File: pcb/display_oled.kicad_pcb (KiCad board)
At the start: 2 copper layers, 38.1 x 19.6 mm, 4 parts, among them J1 Molex-50511, Q1 AO3413, U1 SSD1306

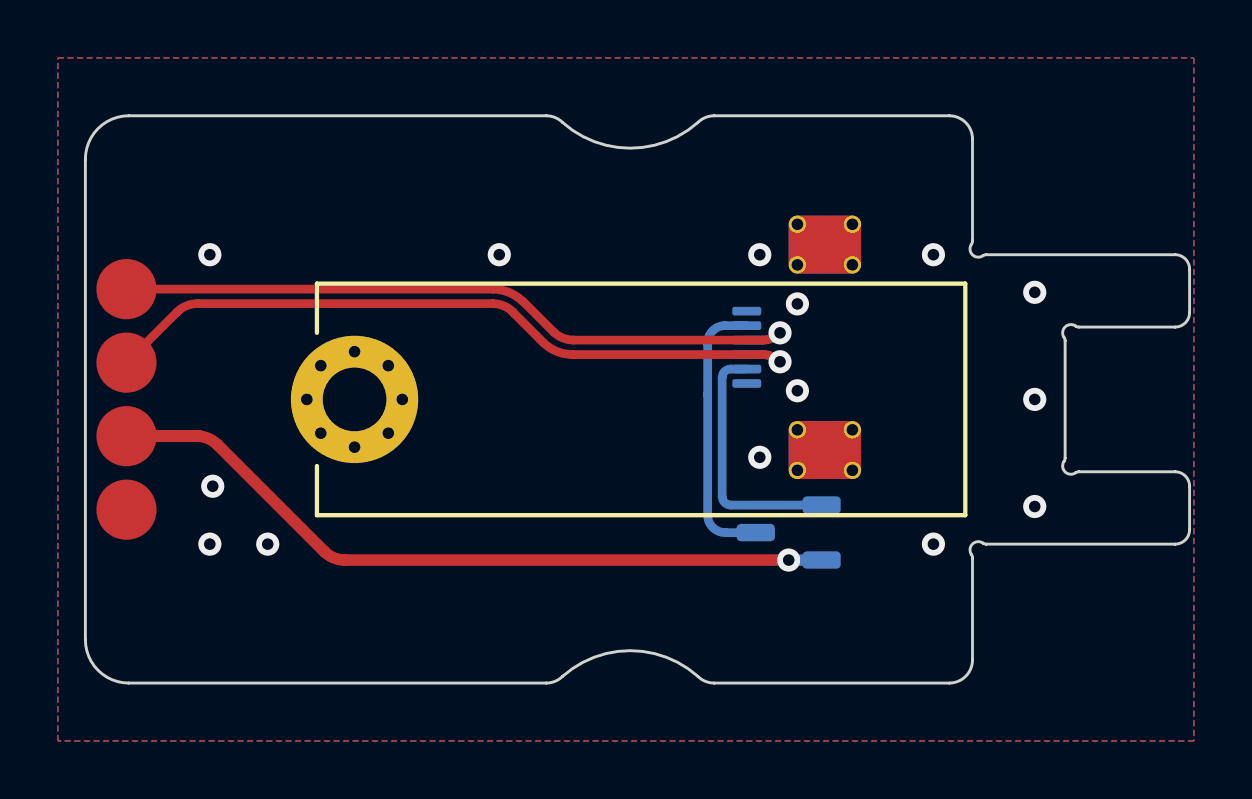
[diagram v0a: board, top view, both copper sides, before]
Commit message: Use KiCad SOT-23-3 footprint
The copied footprint was likely due to a missing 3D model, but the
current KiCad library has a 3D model now.
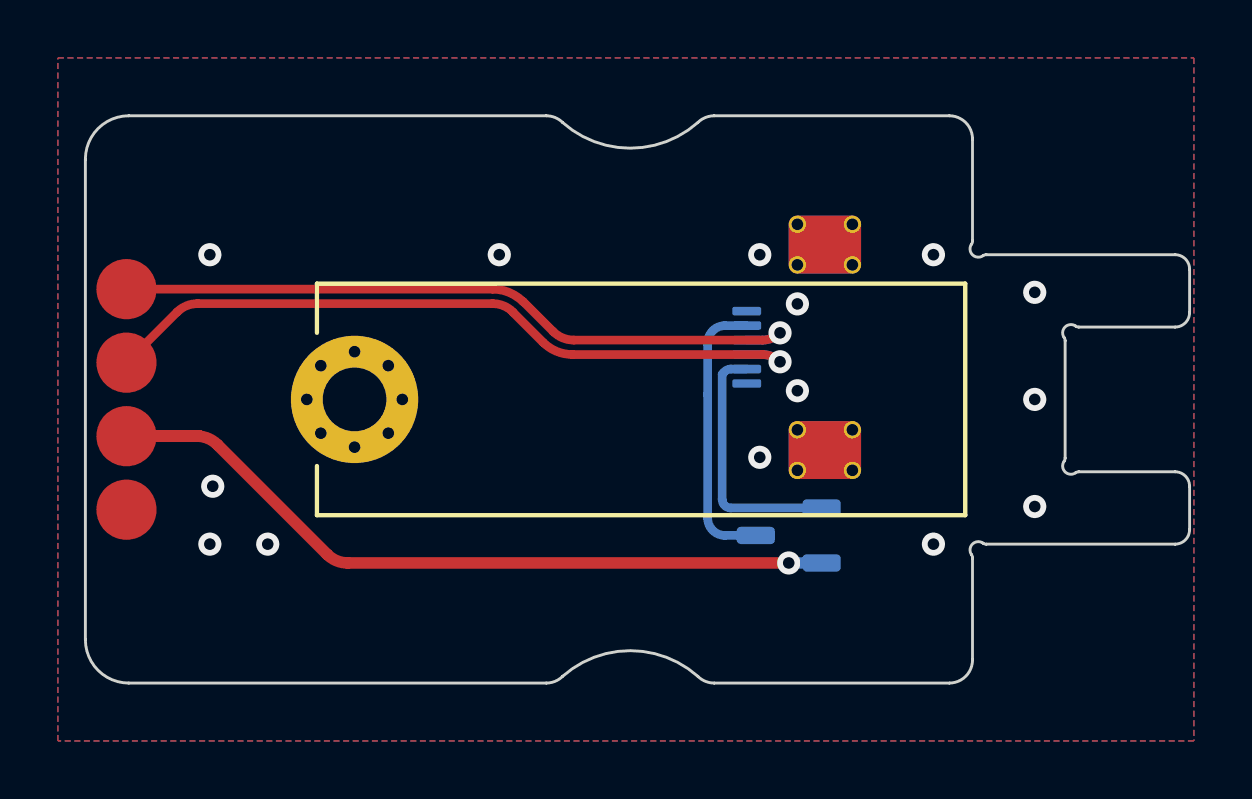
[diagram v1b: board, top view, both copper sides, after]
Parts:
- Q1: footprint keyboard:SOT-23-3 -> Package_TO_SOT_SMD:SOT-23-3
- moved Q1 0.10 mm to (115.0, 104.7)
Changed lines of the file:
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@@
 		)
 	)
-	(footprint "keyboard:SOT-23-3"
+	(footprint "Package_TO_SOT_SMD:SOT-23-3"
 		(layer "B.Cu")
-		(at 115 104.6 180)
+		(at 115 104.7 180)
 		(descr "SOT, 3 Pin (https://www.jedec.org/sites/default/files/docs/Mo-178D.PDF inferred 3-pin variant), generated with kicad-footprint-generator ipc_gullwing_generator.py")
 		(tags "SOT TO_SOT_SMD")
 		(property "Reference" "Q1"
-			(at -2.7 0 90)
+			(at -2.9 0 90)
 			(layer "B.SilkS")
 			(effects
@@
 			)
 		)
-		(property "Footprint" "keyboard:SOT-23-3"
-			(at 0 0 180)
-			(layer "F.Fab")
+		(property "Footprint" "Package_TO_SOT_SMD:SOT-23-3"
+			(at 0 0 0)
+			(unlocked yes)
+			(layer "B.Fab")
 			(hide yes)
 			(effects
@@
 					(thickness 0.15)
 				)
+				(justify mirror)
 			)
 		)
 		(property "Datasheet" ""
-			(at 0 0 180)
-			(layer "F.Fab")
+			(at 0 0 0)
+			(unlocked yes)
+			(layer "B.Fab")
 			(hide yes)
 			(effects
@@
 					(thickness 0.15)
 				)
+				(justify mirror)
 			)
 		)
 		(property "Description" ""
-			(at 0 0 180)
-			(layer "F.Fab")
+			(at 0 0 0)
+			(unlocked yes)
+			(layer "B.Fab")
 			(hide yes)
 			(effects
@@
 					(thickness 0.15)
 				)
+				(justify mirror)
 			)
 		)
@@
 		)
 		(fp_line
+			(start -0.8 1.56)
+			(end 0 1.56)
+			(stroke
+				(width 0.12)
+				(type solid)
+			)
+			(layer "B.SilkS")
+		)
+		(fp_line
 			(start -0.8 -1.56)
 			(end 0 -1.56)
@@
 			(layer "B.SilkS")
 		)
-		(fp_line
-			(start -1.8 1.56)
-			(end 0 1.56)
+		(fp_poly
+			(pts
+				(xy -1.3 1.51) (xy -1.54 1.84) (xy -1.06 1.84) (xy -1.3 1.51)
+			)
 			(stroke
 				(width 0.12)
 				(type solid)
 			)
+			(fill solid)
 			(layer "B.SilkS")
 		)
@@
 			(pintype "passive")
 		)
-		(model "./3dshapes/SOT-23-3.stp"
+		(model "${KICAD8_3DMODEL_DIR}/Package_TO_SOT_SMD.3dshapes/SOT-23-3.wrl"
 			(offset
 				(xyz 0 0 0)
@@
 			)
 			(rotate
-				(xyz 0 0 180)
+				(xyz 0 0 0)
 			)
 		)
@@
 	)
 	(segment
-		(start 112.2 99.85)
-		(end 112.2 104)
+		(start 112.8 104.7)
+		(end 113.8625 104.7)
 		(width 0.3)
 		(layer "B.Cu")
@@
 	)
 	(segment
+		(start 112.2 98.05)
+		(end 112.195919 98.054081)
+		(width 0.3)
+		(layer "B.Cu")
+		(net 2)
+	)
+	(segment
+		(start 113.55 97.45)
+		(end 112.8 97.45)
+		(width 0.3)
+		(layer "B.Cu")
+		(net 2)
+	)
+	(segment
+		(start 112.2 99.85)
+		(end 112.2 104.1)
+		(width 0.3)
+		(layer "B.Cu")
+		(net 2)
+	)
+	(segment
+		(start 112.195919 99.845919)
+		(end 112.2 99.85)
+		(width 0.3)
+		(layer "B.Cu")
+		(net 2)
+	)
+	(segment
 		(start 112.195919 98.054081)
 		(end 112.195919 99.845919)
-		(width 0.3)
-		(layer "B.Cu")
-		(net 2)
-	)
-	(segment
-		(start 113.55 97.45)
-		(end 112.8 97.45)
-		(width 0.3)
-		(layer "B.Cu")
-		(net 2)
-	)
-	(segment
-		(start 112.195919 99.845919)
-		(end 112.2 99.85)
-		(width 0.3)
-		(layer "B.Cu")
-		(net 2)
-	)
-	(segment
-		(start 112.2 98.05)
-		(end 112.195919 98.054081)
-		(width 0.3)
-		(layer "B.Cu")
-		(net 2)
-	)
-	(segment
-		(start 112.8 104.6)
-		(end 113.8625 104.6)
 		(width 0.3)
 		(layer "B.Cu")
@@
 	)
 	(arc
-		(start 112.2 104)
-		(mid 112.375736 104.424264)
-		(end 112.8 104.6)
+		(start 112.2 104.1)
+		(mid 112.375736 104.524264)
+		(end 112.8 104.7)
 		(width 0.3)
 		(layer "B.Cu")
@@
 	)
 	(segment
-		(start 113 103.65)
-		(end 116.1375 103.65)
+		(start 112.748116 99.081696)
+		(end 112.7 99.129812)
 		(width 0.3)
 		(layer "B.Cu")
@@
 	)
 	(segment
-		(start 112.7 99.25)
-		(end 112.7 103.35)
+		(start 113.55 98.95)
+		(end 113 98.95)
 		(width 0.3)
 		(layer "B.Cu")
@@
 	)
 	(segment
-		(start 113.55 98.95)
-		(end 113 98.95)
+		(start 113 103.75)
+		(end 116.1375 103.75)
 		(width 0.3)
 		(layer "B.Cu")
 		(net 5)
 	)
-	(arc
-		(start 112.7 103.35)
-		(mid 112.787868 103.562132)
-		(end 113 103.65)
+	(segment
+		(start 112.7 99.129812)
+		(end 112.7 103.45)
 		(width 0.3)
 		(layer "B.Cu")
@@
 	)
 	(arc
-		(start 113 98.95)
-		(mid 112.787868 99.037868)
-		(end 112.7 99.25)
+		(start 112.7 103.45)
+		(mid 112.787868 103.662132)
+		(end 113 103.75)
 		(width 0.3)
 		(layer "B.Cu")
 		(net 5)
 	)
-	(segment
-		(start 98.957107 105.257107)
-		(end 95.262893 101.562893)
+	(arc
+		(start 113 98.95)
+		(mid 112.858581 98.985424)
+		(end 112.748116 99.081696)
+		(width 0.3)
+		(layer "B.Cu")
+		(net 5)
+	)
+	(segment
+		(start 99.764214 105.65)
+		(end 115 105.65)
 		(width 0.4)
 		(layer "F.Cu")
@@
 	)
 	(segment
-		(start 115 105.55)
-		(end 99.664214 105.55)
-		(width 0.4)
-		(layer "F.Cu")
-		(net 6)
-	)
-	(segment
 		(start 92.171744 101.271744)
 		(end 92.17 101.27)
@@
 		(net 6)
 	)
+	(segment
+		(start 95.262893 101.562893)
+		(end 99.057107 105.357107)
+		(width 0.4)
+		(layer "F.Cu")
+		(net 6)
+	)
 	(via
-		(at 115 105.55)
+		(at 115 105.65)
 		(size 0.8)
 		(drill 0.4)
@@
 	)
 	(arc
-		(start 99.664214 105.55)
-		(mid 99.281531 105.47388)
-		(end 98.957107 105.257107)
+		(start 99.057107 105.357107)
+		(mid 99.38153 105.57388)
+		(end 99.764214 105.65)
 		(width 0.4)
 		(layer "F.Cu")
@@
 	)
 	(arc
-		(start 95.262893 101.562893)
+		(start 94.654106 101.271744)
 		(mid 94.98334 101.366014)
-		(end 94.654106 101.271744)
+		(end 95.262893 101.562893)
 		(width 0.4)
 		(layer "F.Cu")
@@
 	)
 	(segment
-		(start 116.1375 105.55)
-		(end 115 105.55)
+		(start 116.1375 105.65)
+		(end 115 105.65)
 		(width 0.4)
 		(layer "B.Cu")
